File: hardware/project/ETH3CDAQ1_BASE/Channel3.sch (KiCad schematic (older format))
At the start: 2 parts, among them J601 Conn_02x10_Odd_Even, J602 Conn_02x10_Odd_Even

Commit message: PCB layout
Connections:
- net labels added: +18V, +18VF, -18V, -18VF
- net labels removed: +15V, +15VF, -15V, -15VF
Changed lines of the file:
@@
 Comment4 ""
 $EndDescr
-$Comp
-L ETH3CDAQ1:-15VF #PWR?
-U 1 1 602C56F5
-P 4200 3950
-AR Path="/601F1EBA/602C56F5" Ref="#PWR?"  Part="1"
-AR Path="/602C0344/602C56F5" Ref="#PWR0607"  Part="1"
-F 0 "#PWR0607" H 4200 3800 50  0001 C CNN
-F 1 "-15VF" V 4215 4077 50  0000 L CNN
-F 2 "" H 4200 3950 50  0001 C CNN
-F 3 "" H 4200 3950 50  0001 C CNN
-	1    4200 3950
-	0    -1   -1   0
-$EndComp
-$Comp
-L ETH3CDAQ1:+15VF #PWR?
-U 1 1 602C56FB
-P 4800 3950
-AR Path="/601F1EBA/602C56FB" Ref="#PWR?"  Part="1"
-AR Path="/602C0344/602C56FB" Ref="#PWR0612"  Part="1"
-F 0 "#PWR0612" H 4800 3800 50  0001 C CNN
-F 1 "+15VF" V 4815 4078 50  0000 L CNN
-F 2 "" H 4800 3950 50  0001 C CNN
-F 3 "" H 4800 3950 50  0001 C CNN
-	1    4800 3950
-	0    1    1    0
-$EndComp
 Wire Wire Line
 	4800 3950 4750 3950
@@
 Wire Wire Line
 	7250 3850 7300 3850
-$Comp
-L power:+15V #PWR?
-U 1 1 602C5791
-P 7300 3950
-AR Path="/601F1EBA/602C5791" Ref="#PWR?"  Part="1"
-AR Path="/602C0344/602C5791" Ref="#PWR0624"  Part="1"
-F 0 "#PWR0624" H 7300 3800 50  0001 C CNN
-F 1 "+15V" V 7315 4078 50  0000 L CNN
-F 2 "" H 7300 3950 50  0001 C CNN
-F 3 "" H 7300 3950 50  0001 C CNN
-	1    7300 3950
-	0    1    1    0
-$EndComp
-$Comp
-L power:-15V #PWR?
-U 1 1 602C5797
-P 6700 3950
-AR Path="/601F1EBA/602C5797" Ref="#PWR?"  Part="1"
-AR Path="/602C0344/602C5797" Ref="#PWR0619"  Part="1"
-F 0 "#PWR0619" H 6700 4050 50  0001 C CNN
-F 1 "-15V" V 6715 4078 50  0000 L CNN
-F 2 "" H 6700 3950 50  0001 C CNN
-F 3 "" H 6700 3950 50  0001 C CNN
-	1    6700 3950
-	0    -1   -1   0
-$EndComp
 Wire Wire Line
 	4250 3550 3550 3550
@@
 	0    -1   -1   0
 $EndComp
+$Comp
+L ETH3CDAQ1:-18VF #PWR0607
+U 1 1 5FB72157
+P 4200 3950
+F 0 "#PWR0607" H 4200 3800 50  0001 C CNN
+F 1 "-18VF" V 4200 4100 50  0000 L CNN
+F 2 "" H 4200 3950 50  0001 C CNN
+F 3 "" H 4200 3950 50  0001 C CNN
+	1    4200 3950
+	0    -1   -1   0
+$EndComp
+$Comp
+L ETH3CDAQ1:+18VF #PWR0612
+U 1 1 5FB72A8C
+P 4800 3950
+F 0 "#PWR0612" H 4800 3800 50  0001 C CNN
+F 1 "+18VF" V 4800 4100 50  0000 L CNN
+F 2 "" H 4800 3950 50  0001 C CNN
+F 3 "" H 4800 3950 50  0001 C CNN
+	1    4800 3950
+	0    1    1    0
+$EndComp
+$Comp
+L ETH3CDAQ1:-18V #PWR0105
+U 1 1 6002CE58
+P 6700 3950
+F 0 "#PWR0105" H 6700 3800 50  0001 C CNN
+F 1 "-18V" V 6700 4100 50  0000 L CNN
+F 2 "" H 6700 3950 50  0001 C CNN
+F 3 "" H 6700 3950 50  0001 C CNN
+	1    6700 3950
+	0    -1   -1   0
+$EndComp
+$Comp
+L ETH3CDAQ1:+18V #PWR0106
+U 1 1 6002D55A
+P 7300 3950
+F 0 "#PWR0106" H 7300 3800 50  0001 C CNN
+F 1 "+18V" V 7300 4100 50  0000 L CNN
+F 2 "" H 7300 3950 50  0001 C CNN
+F 3 "" H 7300 3950 50  0001 C CNN
+	1    7300 3950
+	0    1    1    0
+$EndComp
 $EndSCHEMATC

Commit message: PCB layout
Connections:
- net +3V3: no longer J602.1 (Pin_1), J602.3 (Pin_3)
- net GND: now also J602.1 (Pin_1), J602.3 (Pin_3)
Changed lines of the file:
@@
 Wire Wire Line
 	4800 3750 4750 3750
-$Comp
-L power:+3.3V #PWR?
-U 1 1 602C5782
-P 6700 3150
-AR Path="/601F1EBA/602C5782" Ref="#PWR?"  Part="1"
-AR Path="/602C0344/602C5782" Ref="#PWR0614"  Part="1"
-F 0 "#PWR0614" H 6700 3000 50  0001 C CNN
-F 1 "+3.3V" V 6700 3300 50  0000 L CNN
-F 2 "" H 6700 3150 50  0001 C CNN
-F 3 "" H 6700 3150 50  0001 C CNN
-	1    6700 3150
-	0    -1   -1   0
-$EndComp
-$Comp
-L power:+3.3V #PWR?
-U 1 1 602C5788
-P 6700 3050
-AR Path="/601F1EBA/602C5788" Ref="#PWR?"  Part="1"
-AR Path="/602C0344/602C5788" Ref="#PWR0613"  Part="1"
-F 0 "#PWR0613" H 6700 2900 50  0001 C CNN
-F 1 "+3.3V" V 6700 3200 50  0000 L CNN
-F 2 "" H 6700 3050 50  0001 C CNN
-F 3 "" H 6700 3050 50  0001 C CNN
-	1    6700 3050
-	0    -1   -1   0
-$EndComp
 Wire Wire Line
 	6700 3750 6750 3750
@@
 	0    1    1    0
 $EndComp
+$Comp
+L power:GND #PWR?
+U 1 1 5FCDD692
+P 6700 3150
+AR Path="/601F1EBA/5FCDD692" Ref="#PWR?"  Part="1"
+AR Path="/602C0344/5FCDD692" Ref="#PWR?"  Part="1"
+F 0 "#PWR?" H 6700 2900 50  0001 C CNN
+F 1 "GND" V 6705 3022 50  0000 R CNN
+F 2 "" H 6700 3150 50  0001 C CNN
+F 3 "" H 6700 3150 50  0001 C CNN
+	1    6700 3150
+	0    1    1    0
+$EndComp
+$Comp
+L power:GND #PWR?
+U 1 1 5FCDDA59
+P 6700 3050
+AR Path="/601F1EBA/5FCDDA59" Ref="#PWR?"  Part="1"
+AR Path="/602C0344/5FCDDA59" Ref="#PWR?"  Part="1"
+F 0 "#PWR?" H 6700 2800 50  0001 C CNN
+F 1 "GND" V 6705 2922 50  0000 R CNN
+F 2 "" H 6700 3050 50  0001 C CNN
+F 3 "" H 6700 3050 50  0001 C CNN
+	1    6700 3050
+	0    1    1    0
+$EndComp

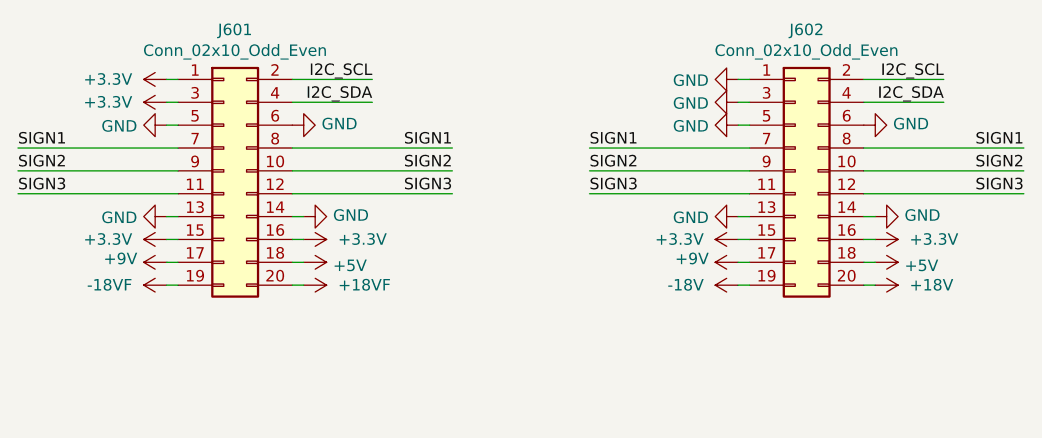
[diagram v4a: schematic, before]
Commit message: Voltage front-end development
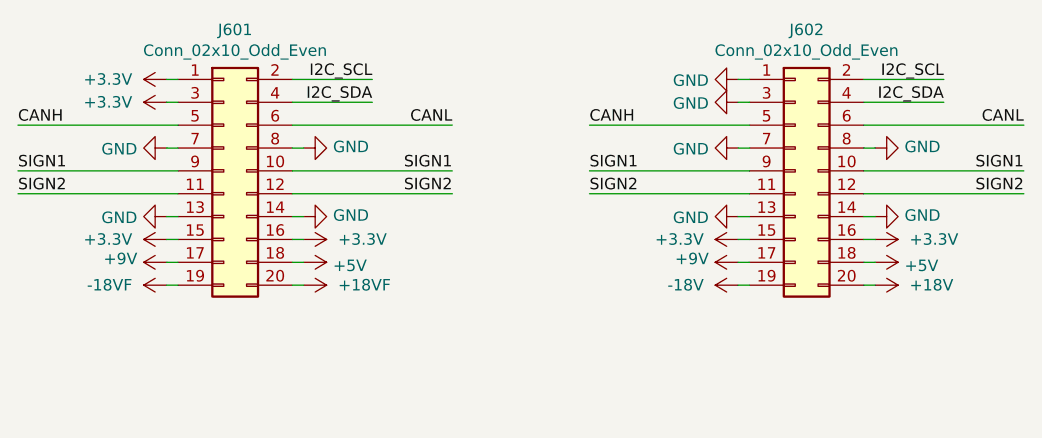
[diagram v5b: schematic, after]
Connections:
- net SIGN3 is gone; now on net SIGN2: J601.11 (Pin_11), J601.12 (Pin_12), J602.11 (Pin_11), J602.12 (Pin_12)
- net GND: now also J601.7 (Pin_7), J601.8 (Pin_8), J602.7 (Pin_7), J602.8 (Pin_8); no longer J601.5 (Pin_5), J601.6 (Pin_6), J602.5 (Pin_5), J602.6 (Pin_6)
- net SIGN1: now also J601.10 (Pin_10), J601.9 (Pin_9), J602.10 (Pin_10), J602.9 (Pin_9); no longer J601.7 (Pin_7), J601.8 (Pin_8), J602.7 (Pin_7), J602.8 (Pin_8)
- net SIGN2: no longer J601.10 (Pin_10), J601.9 (Pin_9), J602.10 (Pin_10), J602.9 (Pin_9)
- new net CANH: J601.5 (Pin_5), J602.5 (Pin_5)
- new net CANL: J601.6 (Pin_6), J602.6 (Pin_6)
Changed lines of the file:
@@
 	0    -1   -1   0
-$EndComp
-$Comp
-L power:GND #PWR?
-U 1 1 602C5733
-P 4200 3250
-AR Path="/601F1EBA/602C5733" Ref="#PWR?"  Part="1"
-AR Path="/602C0344/602C5733" Ref="#PWR0603"  Part="1"
-F 0 "#PWR0603" H 4200 3000 50  0001 C CNN
-F 1 "GND" V 4205 3122 50  0000 R CNN
-F 2 "" H 4200 3250 50  0001 C CNN
-F 3 "" H 4200 3250 50  0001 C CNN
-	1    4200 3250
-	0    1    1    0
 $EndComp
 Wire Wire Line
@@
 	4250 3450 3550 3450
 Text Label 3550 3450 0    50   ~ 0
-SIGN2
+SIGN1
 Wire Wire Line
 	7250 3050 7600 3050
@@
 	4800 3650 4750 3650
 Wire Wire Line
-	4250 3250 4200 3250
-Wire Wire Line
 	4200 3150 4250 3150
 Wire Wire Line
@@
 Wire Wire Line
 	6750 3150 6700 3150
-Wire Wire Line
-	6700 3250 6750 3250
 $Comp
 L power:+3.3V #PWR?
@@
 	4250 3550 3550 3550
 Text Label 3550 3550 0    50   ~ 0
-SIGN3
+SIGN2
 Wire Wire Line
 	6700 3650 6750 3650
@@
 	7250 3650 7300 3650
 Wire Wire Line
-	4250 3350 3550 3350
-Text Label 3550 3350 0    50   ~ 0
-SIGN1
-$Comp
-L power:GND #PWR?
-U 1 1 602C57A3
-P 4750 3250
-AR Path="/601F1EBA/602C57A3" Ref="#PWR?"  Part="1"
-AR Path="/602C0344/602C57A3" Ref="#PWR0608"  Part="1"
-F 0 "#PWR0608" H 4750 3000 50  0001 C CNN
-F 1 "GND" V 4755 3122 50  0000 R CNN
-F 2 "" H 4750 3250 50  0001 C CNN
-F 3 "" H 4750 3250 50  0001 C CNN
-	1    4750 3250
-	0    -1   -1   0
-$EndComp
-$Comp
-L power:GND #PWR?
-U 1 1 602C57A9
-P 6700 3250
-AR Path="/601F1EBA/602C57A9" Ref="#PWR?"  Part="1"
-AR Path="/602C0344/602C57A9" Ref="#PWR0615"  Part="1"
-F 0 "#PWR0615" H 6700 3000 50  0001 C CNN
-F 1 "GND" V 6705 3122 50  0000 R CNN
-F 2 "" H 6700 3250 50  0001 C CNN
-F 3 "" H 6700 3250 50  0001 C CNN
-	1    6700 3250
-	0    1    1    0
-$EndComp
-$Comp
-L power:GND #PWR?
-U 1 1 602C57AF
-P 7250 3250
-AR Path="/601F1EBA/602C57AF" Ref="#PWR?"  Part="1"
-AR Path="/602C0344/602C57AF" Ref="#PWR0620"  Part="1"
-F 0 "#PWR0620" H 7250 3000 50  0001 C CNN
-F 1 "GND" V 7255 3122 50  0000 R CNN
-F 2 "" H 7250 3250 50  0001 C CNN
-F 3 "" H 7250 3250 50  0001 C CNN
-	1    7250 3250
-	0    -1   -1   0
-$EndComp
+	4250 3250 3550 3250
+Text Label 3550 3250 0    50   ~ 0
+CANH
 Wire Wire Line
 	4750 3450 5450 3450
 Text Label 5450 3450 2    50   ~ 0
-SIGN2
+SIGN1
 Wire Wire Line
 	4750 3550 5450 3550
 Text Label 5450 3550 2    50   ~ 0
-SIGN3
-Wire Wire Line
-	4750 3350 5450 3350
-Text Label 5450 3350 2    50   ~ 0
-SIGN1
+SIGN2
+Wire Wire Line
+	4750 3250 5450 3250
+Text Label 5450 3250 2    50   ~ 0
+CANL
 Wire Wire Line
 	6750 3450 6050 3450
 Text Label 6050 3450 0    50   ~ 0
-SIGN2
+SIGN1
 Wire Wire Line
 	6750 3550 6050 3550
 Text Label 6050 3550 0    50   ~ 0
-SIGN3
-Wire Wire Line
-	6750 3350 6050 3350
-Text Label 6050 3350 0    50   ~ 0
-SIGN1
+SIGN2
+Wire Wire Line
+	6750 3250 6050 3250
+Text Label 6050 3250 0    50   ~ 0
+CANH
 Wire Wire Line
 	7250 3450 7950 3450
 Text Label 7950 3450 2    50   ~ 0
-SIGN2
+SIGN1
 Wire Wire Line
 	7250 3550 7950 3550
 Text Label 7950 3550 2    50   ~ 0
-SIGN3
-Wire Wire Line
-	7250 3350 7950 3350
-Text Label 7950 3350 2    50   ~ 0
-SIGN1
+SIGN2
+Wire Wire Line
+	7250 3250 7950 3250
+Text Label 7950 3250 2    50   ~ 0
+CANL
 $Comp
 L power:+3.3V #PWR?
@@
 	0    1    1    0
 $EndComp
+$Comp
+L power:GND #PWR?
+U 1 1 5FD1AEAD
+P 4200 3350
+AR Path="/601F1EBA/5FD1AEAD" Ref="#PWR?"  Part="1"
+AR Path="/602C0344/5FD1AEAD" Ref="#PWR0603"  Part="1"
+F 0 "#PWR0603" H 4200 3100 50  0001 C CNN
+F 1 "GND" V 4205 3222 50  0000 R CNN
+F 2 "" H 4200 3350 50  0001 C CNN
+F 3 "" H 4200 3350 50  0001 C CNN
+	1    4200 3350
+	0    1    1    0
+$EndComp
+Wire Wire Line
+	4200 3350 4250 3350
+Wire Wire Line
+	4750 3350 4800 3350
+$Comp
+L power:GND #PWR?
+U 1 1 5FD1D162
+P 4800 3350
+AR Path="/601F1EBA/5FD1D162" Ref="#PWR?"  Part="1"
+AR Path="/602C0344/5FD1D162" Ref="#PWR0608"  Part="1"
+F 0 "#PWR0608" H 4800 3100 50  0001 C CNN
+F 1 "GND" V 4805 3222 50  0000 R CNN
+F 2 "" H 4800 3350 50  0001 C CNN
+F 3 "" H 4800 3350 50  0001 C CNN
+	1    4800 3350
+	0    -1   -1   0
+$EndComp
+$Comp
+L power:GND #PWR?
+U 1 1 5FD2714F
+P 6700 3350
+AR Path="/601F1EBA/5FD2714F" Ref="#PWR?"  Part="1"
+AR Path="/602C0344/5FD2714F" Ref="#PWR0615"  Part="1"
+F 0 "#PWR0615" H 6700 3100 50  0001 C CNN
+F 1 "GND" V 6705 3222 50  0000 R CNN
+F 2 "" H 6700 3350 50  0001 C CNN
+F 3 "" H 6700 3350 50  0001 C CNN
+	1    6700 3350
+	0    1    1    0
+$EndComp
+Wire Wire Line
+	6700 3350 6750 3350
+$Comp
+L power:GND #PWR?
+U 1 1 5FD286B0
+P 7300 3350
+AR Path="/601F1EBA/5FD286B0" Ref="#PWR?"  Part="1"
+AR Path="/602C0344/5FD286B0" Ref="#PWR0619"  Part="1"
+F 0 "#PWR0619" H 7300 3100 50  0001 C CNN
+F 1 "GND" V 7305 3222 50  0000 R CNN
+F 2 "" H 7300 3350 50  0001 C CNN
+F 3 "" H 7300 3350 50  0001 C CNN
+	1    7300 3350
+	0    -1   -1   0
+$EndComp
+Wire Wire Line
+	7300 3350 7250 3350
 $EndSCHEMATC

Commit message: Added selftest circuit in the base PCB.
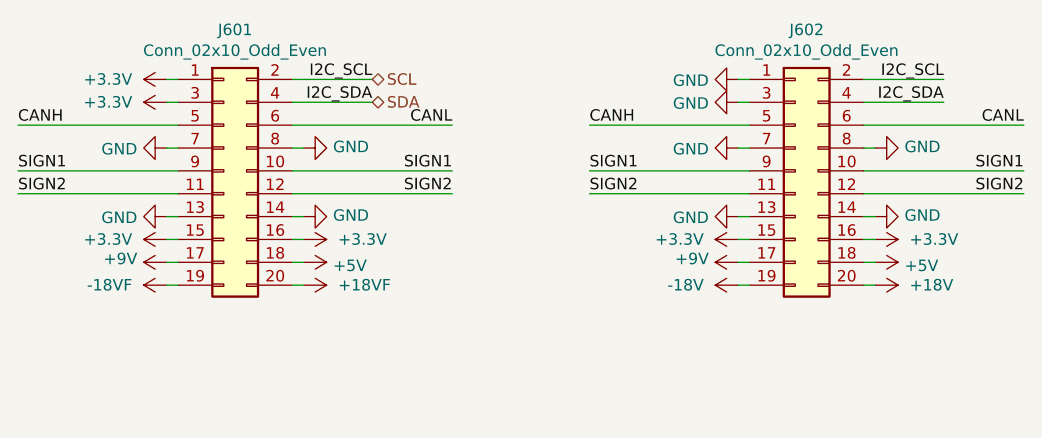
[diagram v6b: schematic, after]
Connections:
- net I2C_SCL renamed SCL
- net I2C_SDA renamed SDA
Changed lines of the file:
@@
 $Descr A4 11693 8268
 encoding utf-8
-Sheet 6 6
+Sheet 6 7
 Title ""
 Date ""
@@
 $EndComp
 $Comp
-L ETH3CDAQ1:-18V #PWR0105
+L ETH3CDAQ1:-18V #PWR0619
 U 1 1 6002CE58
 P 6700 3950
-F 0 "#PWR0105" H 6700 3800 50  0001 C CNN
+F 0 "#PWR0619" H 6700 3800 50  0001 C CNN
 F 1 "-18V" V 6700 4100 50  0000 L CNN
 F 2 "" H 6700 3950 50  0001 C CNN
@@
 $EndComp
 $Comp
-L ETH3CDAQ1:+18V #PWR0106
+L ETH3CDAQ1:+18V #PWR0624
 U 1 1 6002D55A
 P 7300 3950
-F 0 "#PWR0106" H 7300 3800 50  0001 C CNN
+F 0 "#PWR0624" H 7300 3800 50  0001 C CNN
 F 1 "+18V" V 7300 4100 50  0000 L CNN
 F 2 "" H 7300 3950 50  0001 C CNN
@@
 P 7300 3350
 AR Path="/601F1EBA/5FD286B0" Ref="#PWR?"  Part="1"
-AR Path="/602C0344/5FD286B0" Ref="#PWR0619"  Part="1"
-F 0 "#PWR0619" H 7300 3100 50  0001 C CNN
+AR Path="/602C0344/5FD286B0" Ref="#PWR0620"  Part="1"
+F 0 "#PWR0620" H 7300 3100 50  0001 C CNN
 F 1 "GND" V 7305 3222 50  0000 R CNN
 F 2 "" H 7300 3350 50  0001 C CNN
@@
 Wire Wire Line
 	7300 3350 7250 3350
+Text HLabel 5100 3050 2    50   BiDi ~ 0
+SCL
+Text HLabel 5100 3150 2    50   BiDi ~ 0
+SDA
 $EndSCHEMATC
